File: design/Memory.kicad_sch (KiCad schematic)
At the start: 10 parts, among them U14 SST39SF040, U15 SST39SF040, U16 AS6C4008-55PCN, U17 AS6C4008-55PCN

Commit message: Fix all R/C part numbers: switch to JLCPCB basic parts, correct footprints
- Replace all non-basic LCSC numbers with JLCPCB basic equivalents (no
  extended part setup fees): Samsung MLCCs for caps, UNI-ROYAL 0805W8F
  series for resistors
- Fix C49 footprint: 1210 → 1206 to match Samsung CL31A476MPHNNNE
- Correct previously wrong LCSC numbers (C17512→C17513, C17515→C17673,
  C135808→C96123) and missing R17 part numbers
- Update all Mouser numbers to match the LCSC manufacturer throughout
- Standardise all resistor footprints to HandSolder pad variant
- Update datasheets/INDEX.md with verified basic part table

Co-Authored-By: Claude Sonnet 4.6 <noreply@anthropic.com>
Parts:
- R20: LCSC C84376 -> C17414; Mouser 603-RC0805FR-0710KL -> 0805W8F1002T5E
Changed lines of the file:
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@@
 			)
 		)
-		(property "Mouser" "603-RC0805FR-0710KL"
+		(property "Mouser" "0805W8F1002T5E "
 			(at 77.47 151.13 0)
 			(hide yes)
@@
 			)
 		)
-		(property "LCSC" "C84376"
+		(property "LCSC" "C17414"
 			(at 77.47 151.13 0)
 			(hide yes)

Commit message: Update IC part numbers: SST39SF040, AS6C4008, LM809M3-4.63/NOPB
- SST39SF040 (U14/U15): Mouser 579-SST39SF040-70-4I-NHE (PLCC-32,
  industrial grade); LCSC has no PLCC-32 variant in stock
- AS6C4008-55PCN (U16/U17): fix LCSC C62646→C1350141 (was invalid/404);
  Mouser 913-AS6C4008-55PCN has stock, LCSC currently OOS
- LM809M3-4.63/NOPB (U11): add LCSC C2066444 and Mouser part number
  properties to schematic

Co-Authored-By: Claude Sonnet 4.6 <noreply@anthropic.com>
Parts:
- U14, U15: Mouser (none) -> SST39SF040-70-4I-NHE
- U16, U17: Mouser (none) -> 913-AS6C4008-55PCN
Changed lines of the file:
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@@
+			)
+		)
+		(property "Mouser" "SST39SF040-70-4I-NHE"
+			(at 55.88 102.87 0)
+			(hide yes)
+			(show_name no)
+			(do_not_autoplace no)
+			(effects
+				(font
+					(size 1.27 1.27)
+				)
 			)
 		)
@@
 			)
 		)
+		(property "Mouser" "913-AS6C4008-55PCN"
+			(at 158.75 96.52 0)
+			(hide yes)
+			(show_name no)
+			(do_not_autoplace no)
+			(effects
+				(font
+					(size 1.27 1.27)
+				)
+			)
+		)
 		(pin "21"
 		)
@@
 			)
 		)
+		(property "Mouser" "SST39SF040-70-4I-NHE"
+			(at 107.95 102.87 0)
+			(hide yes)
+			(show_name no)
+			(do_not_autoplace no)
+			(effects
+				(font
+					(size 1.27 1.27)
+				)
+			)
+		)
 		(pin "21"
 		)
@@
 			(at 210.82 96.52 0)
 			(hide yes)
+			(show_name no)
+			(do_not_autoplace no)
+			(effects
+				(font
+					(size 1.27 1.27)
+				)
+			)
+		)
+		(property "Mouser" "913-AS6C4008-55PCN"
+			(at 210.82 96.52 0)
+			(hide yes)

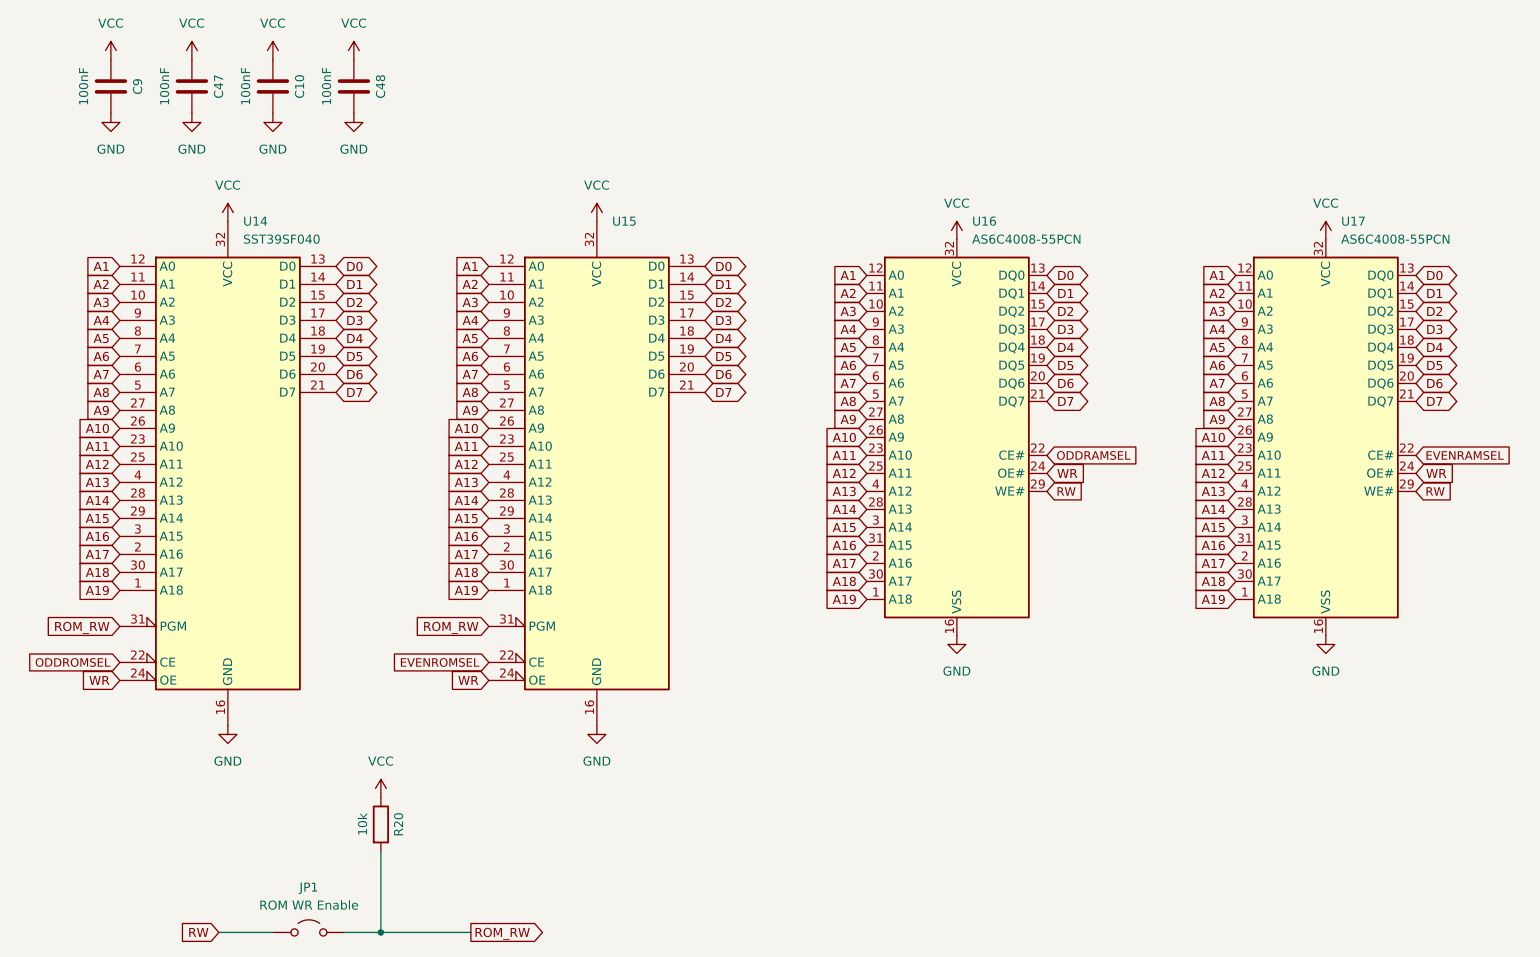
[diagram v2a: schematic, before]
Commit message: Fix even/odd memory bus wiring and route PCB
- Connect U15 (even ROM) and U17 (even RAM) data pins to D8-D15 instead
  of D0-D7: upper byte was completely unconnected, causing half-garbage
  reads and lost writes on all 16-bit accesses
- Reduce R32/R33 LED resistors from 4.7k to 1k (MCP2221A GPIO is 3.3V,
  4.7k gave only 0.26mA — too dim)
- Initial PCB layout and routing

Co-Authored-By: Claude Sonnet 4.6 <noreply@anthropic.com>
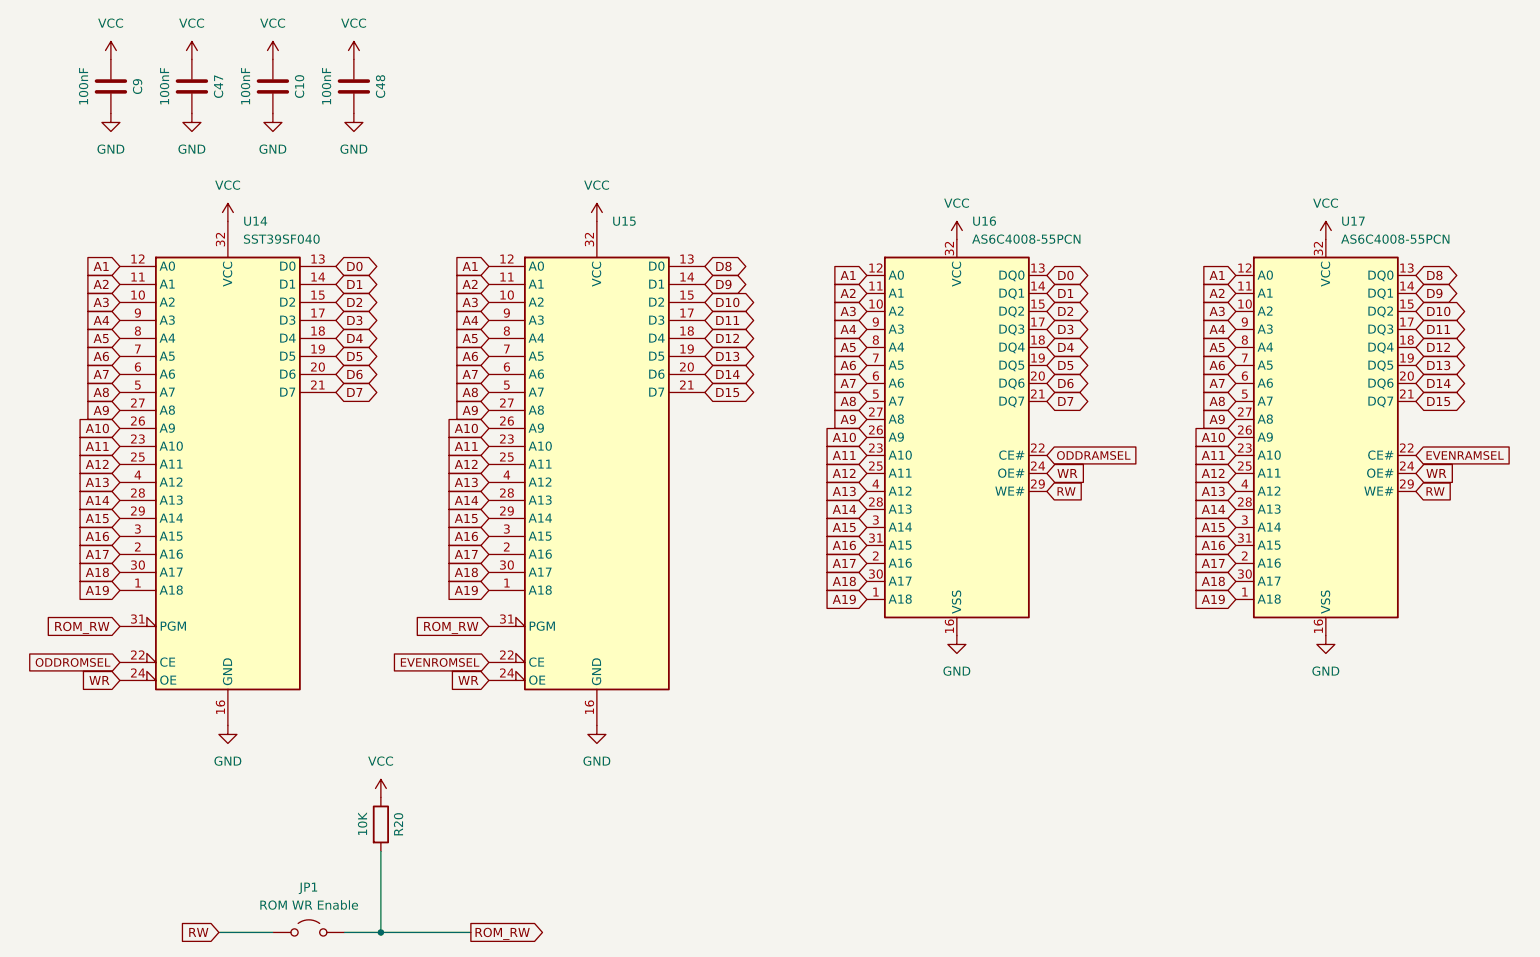
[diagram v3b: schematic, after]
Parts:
- R20: value 10k -> 10K
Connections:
- net D0: no longer U15.13 (D0), U17.13 (DQ0)
- net D1: no longer U15.14 (D1), U17.14 (DQ1)
- net D2: no longer U15.15 (D2), U17.15 (DQ2)
- net D3: no longer U15.17 (D3), U17.17 (DQ3)
- net D4: no longer U15.18 (D4), U17.18 (DQ4)
- net D5: no longer U15.19 (D5), U17.19 (DQ5)
- net D6: no longer U15.20 (D6), U17.20 (DQ6)
- net D7: no longer U15.21 (D7), U17.21 (DQ7)
- new net D10: U15.15 (D2), U17.15 (DQ2)
- new net D11: U15.17 (D3), U17.17 (DQ3)
- new net D12: U15.18 (D4), U17.18 (DQ4)
- new net D13: U15.19 (D5), U17.19 (DQ5)
- new net D14: U15.20 (D6), U17.20 (DQ6)
- new net D15: U15.21 (D7), U17.21 (DQ7)
- new net D8: U15.13 (D0), U17.13 (DQ0)
- new net D9: U15.14 (D1), U17.14 (DQ1)
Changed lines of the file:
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@@
 		)
 	)
-	(global_label "D2"
+	(global_label "D10"
 		(shape bidirectional)
 		(at 123.19 77.47 0)
@@
 		)
 		(property "Intersheetrefs" "${INTERSHEET_REFS}"
-			(at 128.953 77.47 0)
+			(at 130.9755 77.47 0)
 			(hide yes)
 			(show_name yes)
@@
 		)
 	)
-	(global_label "D4"
+	(global_label "D12"
 		(shape bidirectional)
 		(at 223.52 83.82 0)
@@
 		)
 		(property "Intersheetrefs" "${INTERSHEET_REFS}"
-			(at 229.283 83.82 0)
+			(at 231.3055 83.82 0)
 			(hide yes)
 			(show_name yes)
@@
 		)
 	)
-	(global_label "D0"
+	(global_label "D8"
 		(shape bidirectional)
 		(at 223.52 73.66 0)
@@
 		)
 		(property "Intersheetrefs" "${INTERSHEET_REFS}"
-			(at 229.283 73.66 0)
+			(at 230.096 73.66 0)
 			(hide yes)
 			(show_name yes)
@@
 		)
 	)
-	(global_label "D3"
+	(global_label "D11"
 		(shape bidirectional)
 		(at 223.52 81.28 0)
@@
 		)
 		(property "Intersheetrefs" "${INTERSHEET_REFS}"
-			(at 229.283 81.28 0)
+			(at 231.3055 81.28 0)
 			(hide yes)
 			(show_name yes)
@@
 		)
 	)
-	(global_label "D5"
+	(global_label "D13"
 		(shape bidirectional)
 		(at 123.19 85.09 0)
@@
 		)
 		(property "Intersheetrefs" "${INTERSHEET_REFS}"
-			(at 128.953 85.09 0)
+			(at 130.9755 85.09 0)
 			(hide yes)
 			(show_name yes)
@@
 		)
 	)
-	(global_label "D0"
+	(global_label "D8"
 		(shape bidirectional)
 		(at 123.19 72.39 0)
@@
 		)
 		(property "Intersheetrefs" "${INTERSHEET_REFS}"
-			(at 128.953 72.39 0)
+			(at 129.766 72.39 0)
 			(hide yes)
 			(show_name yes)
@@
 		)
 	)
-	(global_label "D7"
+	(global_label "D15"
 		(shape bidirectional)
 		(at 223.52 91.44 0)
@@
 		)
 		(property "Intersheetrefs" "${INTERSHEET_REFS}"
-			(at 229.283 91.44 0)
+			(at 231.3055 91.44 0)
 			(hide yes)
 			(show_name yes)
@@
 		)
 	)
-	(global_label "D6"
+	(global_label "D14"
 		(shape bidirectional)
 		(at 223.52 88.9 0)
@@
 		)
 		(property "Intersheetrefs" "${INTERSHEET_REFS}"
-			(at 229.283 88.9 0)
+			(at 231.3055 88.9 0)
 			(hide yes)
 			(show_name yes)
@@
 		)
 	)
-	(global_label "D7"
+	(global_label "D15"
 		(shape bidirectional)
 		(at 123.19 90.17 0)
@@
 		)
 		(property "Intersheetrefs" "${INTERSHEET_REFS}"
-			(at 128.953 90.17 0)
+			(at 130.9755 90.17 0)
 			(hide yes)
 			(show_name yes)
@@
 		)
 	)
-	(global_label "D5"
+	(global_label "D13"
 		(shape bidirectional)
 		(at 223.52 86.36 0)
@@
 		)
 		(property "Intersheetrefs" "${INTERSHEET_REFS}"
-			(at 229.283 86.36 0)
+			(at 231.3055 86.36 0)
 			(hide yes)
 			(show_name yes)
@@
 		)
 	)
-	(global_label "D4"
+	(global_label "D12"
 		(shape bidirectional)
 		(at 123.19 82.55 0)
@@
 		)
 		(property "Intersheetrefs" "${INTERSHEET_REFS}"
-			(at 128.953 82.55 0)
+			(at 130.9755 82.55 0)
 			(hide yes)
 			(show_name yes)
@@
 		)
 	)
-	(global_label "D6"
+	(global_label "D14"
 		(shape bidirectional)
 		(at 123.19 87.63 0)
@@
 		)
 		(property "Intersheetrefs" "${INTERSHEET_REFS}"
-			(at 128.953 87.63 0)
+			(at 130.9755 87.63 0)
 			(hide yes)
 			(show_name yes)
@@
 		)
 	)
-	(global_label "D1"
+	(global_label "D9"
 		(shape bidirectional)
 		(at 223.52 76.2 0)
@@
 		)
 		(property "Intersheetrefs" "${INTERSHEET_REFS}"
-			(at 229.283 76.2 0)
+			(at 230.096 76.2 0)
 			(hide yes)
 			(show_name yes)
@@
 		)
 	)
-	(global_label "D1"
+	(global_label "D9"
 		(shape bidirectional)
 		(at 123.19 74.93 0)
@@
 		)
 		(property "Intersheetrefs" "${INTERSHEET_REFS}"
-			(at 128.953 74.93 0)
+			(at 129.766 74.93 0)
 			(hide yes)
 			(show_name yes)
@@
 		)
 	)
-	(global_label "D3"
+	(global_label "D11"
 		(shape bidirectional)
 		(at 123.19 80.01 0)
@@
 		)
 		(property "Intersheetrefs" "${INTERSHEET_REFS}"
-			(at 128.953 80.01 0)
+			(at 130.9755 80.01 0)
 			(hide yes)
 			(show_name yes)
@@
 		)
 	)
-	(global_label "D2"
+	(global_label "D10"
 		(shape bidirectional)
 		(at 223.52 78.74 0)
@@
 		)
 		(property "Intersheetrefs" "${INTERSHEET_REFS}"
-			(at 229.283 78.74 0)
+			(at 231.3055 78.74 0)
 			(hide yes)
 			(show_name yes)
@@
 			)
 		)
-		(property "Value" "10k"
+		(property "Value" "10K"
 			(at 74.93 151.13 90)
 			(show_name no)

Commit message: Update KiCad design files and add fabrication outputs
Schematic and PCB updates including component renumbering (ICs, passives,
LEDs, oscillators). Add JLCPCB fabrication toolkit settings and v1
production outputs (gerbers zip, IPC netlist).

Co-Authored-By: Claude Sonnet 4.6 <noreply@anthropic.com>
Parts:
- renumbered C9 to C5, C47 to C6, C10 to C7, C48 to C8, R20 to R2, U14 to U3, U15 to U4, U16 to U5, U17 to U6
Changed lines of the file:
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@@
 		(dnp no)
 		(fields_autoplaced yes)
-		(property "Reference" "U14"
+		(property "Reference" "U3"
 			(at 58.0233 66.04 0)
 			(show_name no)
@@
 			(project "Simple010"
 				(path "/4f37455c-e998-4ed3-8493-a94956af64c1/d43ba676-34f7-491a-b472-bfb93379ede2"
-					(reference "U14")
+					(reference "U3")
 					(unit 1)
 				)
@@
 		(in_pos_files yes)
 		(dnp no)
-		(property "Reference" "R20"
+		(property "Reference" "R2"
 			(at 80.01 151.13 90)
 			(show_name no)
@@
 			(project "Simple010"
 				(path "/4f37455c-e998-4ed3-8493-a94956af64c1/d43ba676-34f7-491a-b472-bfb93379ede2"
-					(reference "R20")
+					(reference "R2")
 					(unit 1)
 				)
@@
 		(dnp no)
 		(fields_autoplaced yes)
-		(property "Reference" "U16"
+		(property "Reference" "U5"
 			(at 160.8933 66.04 0)
 			(show_name no)
@@
 			(project "Simple010"
 				(path "/4f37455c-e998-4ed3-8493-a94956af64c1/d43ba676-34f7-491a-b472-bfb93379ede2"
-					(reference "U16")
+					(reference "U5")
 					(unit 1)
 				)
@@
 		(in_pos_files yes)
 		(dnp no)
-		(property "Reference" "C10"
+		(property "Reference" "C7"
 			(at 66.04 46.99 90)
 			(show_name no)
@@
 			(project "Simple010"
 				(path "/4f37455c-e998-4ed3-8493-a94956af64c1/d43ba676-34f7-491a-b472-bfb93379ede2"
-					(reference "C10")
+					(reference "C7")
 					(unit 1)
 				)
@@
 		(dnp no)
 		(fields_autoplaced yes)
-		(property "Reference" "U15"
+		(property "Reference" "U4"
 			(at 110.0933 66.04 0)
 			(show_name no)
@@
 			(project "Simple010"
 				(path "/4f37455c-e998-4ed3-8493-a94956af64c1/d43ba676-34f7-491a-b472-bfb93379ede2"
-					(reference "U15")
+					(reference "U4")
 					(unit 1)
 				)
@@
 		(in_pos_files yes)
 		(dnp no)
-		(property "Reference" "C47"
+		(property "Reference" "C6"
 			(at 54.61 46.99 90)
 			(show_name no)
@@
 			(project "Simple010"
 				(path "/4f37455c-e998-4ed3-8493-a94956af64c1/d43ba676-34f7-491a-b472-bfb93379ede2"
-					(reference "C47")
+					(reference "C6")
 					(unit 1)
 				)
@@
 		(in_pos_files yes)
 		(dnp no)
-		(property "Reference" "C9"
+		(property "Reference" "C5"
 			(at 43.18 46.99 90)
 			(show_name no)
@@
 			(project "Simple010"
 				(path "/4f37455c-e998-4ed3-8493-a94956af64c1/d43ba676-34f7-491a-b472-bfb93379ede2"
-					(reference "C9")
+					(reference "C5")
 					(unit 1)
 				)
@@
 		(in_pos_files yes)
 		(dnp no)
-		(property "Reference" "C48"
+		(property "Reference" "C8"
 			(at 77.47 46.99 90)
 			(show_name no)
@@
 			(project "Simple010"
 				(path "/4f37455c-e998-4ed3-8493-a94956af64c1/d43ba676-34f7-491a-b472-bfb93379ede2"
-					(reference "C48")
+					(reference "C8")
 					(unit 1)
 				)
@@
 		(dnp no)
 		(fields_autoplaced yes)
-		(property "Reference" "U17"
+		(property "Reference" "U6"
 			(at 212.9633 66.04 0)
 			(show_name no)
@@
 			(project "Simple010"
 				(path "/4f37455c-e998-4ed3-8493-a94956af64c1/d43ba676-34f7-491a-b472-bfb93379ede2"
-					(reference "U17")
+					(reference "U6")
 					(unit 1)
 				)
